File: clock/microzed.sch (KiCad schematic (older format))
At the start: 2 parts

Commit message: Update parts with parameter detail and BOM information.
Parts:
- PX1, PX2: Manufacturer (none) -> FCI; PartNum (none) -> 61083-101400LF
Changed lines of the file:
@@
 $Descr A4 11693 8268
 encoding utf-8
-Sheet 5 5
+Sheet 4 5
 Title ""
 Date ""
@@
 Comment4 ""
 $EndDescr
-$Comp
-L 61083_02X50 PX2
-U 1 1 5623D9A9
-P 5250 3750
-F 0 "PX2" H 5250 6400 50  0000 C CNN
-F 1 "61083_02X50" V 5250 3750 50  0000 C CNN
-F 2 "" H 5200 4250 60  0000 C CNN
-F 3 "" H 5200 4250 60  0000 C CNN
-	1    5250 3750
-	1    0    0    -1
-$EndComp
-$Comp
-L 61083_02X50 PX1
-U 1 1 5623D9E8
-P 2300 3750
-F 0 "PX1" H 2300 6400 50  0000 C CNN
-F 1 "61083_02X50" V 2300 3750 50  0000 C CNN
-F 2 "" H 2250 4250 60  0000 C CNN
-F 3 "" H 2250 4250 60  0000 C CNN
-	1    2300 3750
-	1    0    0    -1
-$EndComp
 $Comp
 L GND #PWR?
@@
 NoConn ~ 2000 5700
 NoConn ~ 2000 5600
+$Comp
+L 61083_02X50 PX2
+U 1 1 5633065B
+P 5250 3750
+F 0 "PX2" H 5250 6400 50  0000 C CNN
+F 1 "61083_02X50" V 5250 3750 50  0000 C CNN
+F 2 "" H 5200 4250 60  0000 C CNN
+F 3 "" H 5200 4250 60  0000 C CNN
+F 4 "FCI" H 5250 6600 50  0001 C CNN "Manufacturer"
+F 5 "61083-101400LF" H 5250 6500 50  0001 C CNN "PartNum"
+	1    5250 3750
+	1    0    0    -1
+$EndComp
+$Comp
+L 61083_02X50 PX1
+U 1 1 5633070F
+P 2300 3750
+F 0 "PX1" H 2300 6400 50  0000 C CNN
+F 1 "61083_02X50" V 2300 3750 50  0000 C CNN
+F 2 "" H 2250 4250 60  0000 C CNN
+F 3 "" H 2250 4250 60  0000 C CNN
+F 4 "FCI" H 2300 6600 50  0001 C CNN "Manufacturer"
+F 5 "61083-101400LF" H 2300 6500 50  0001 C CNN "PartNum"
+	1    2300 3750
+	1    0    0    -1
+$EndComp
 $EndSCHEMATC

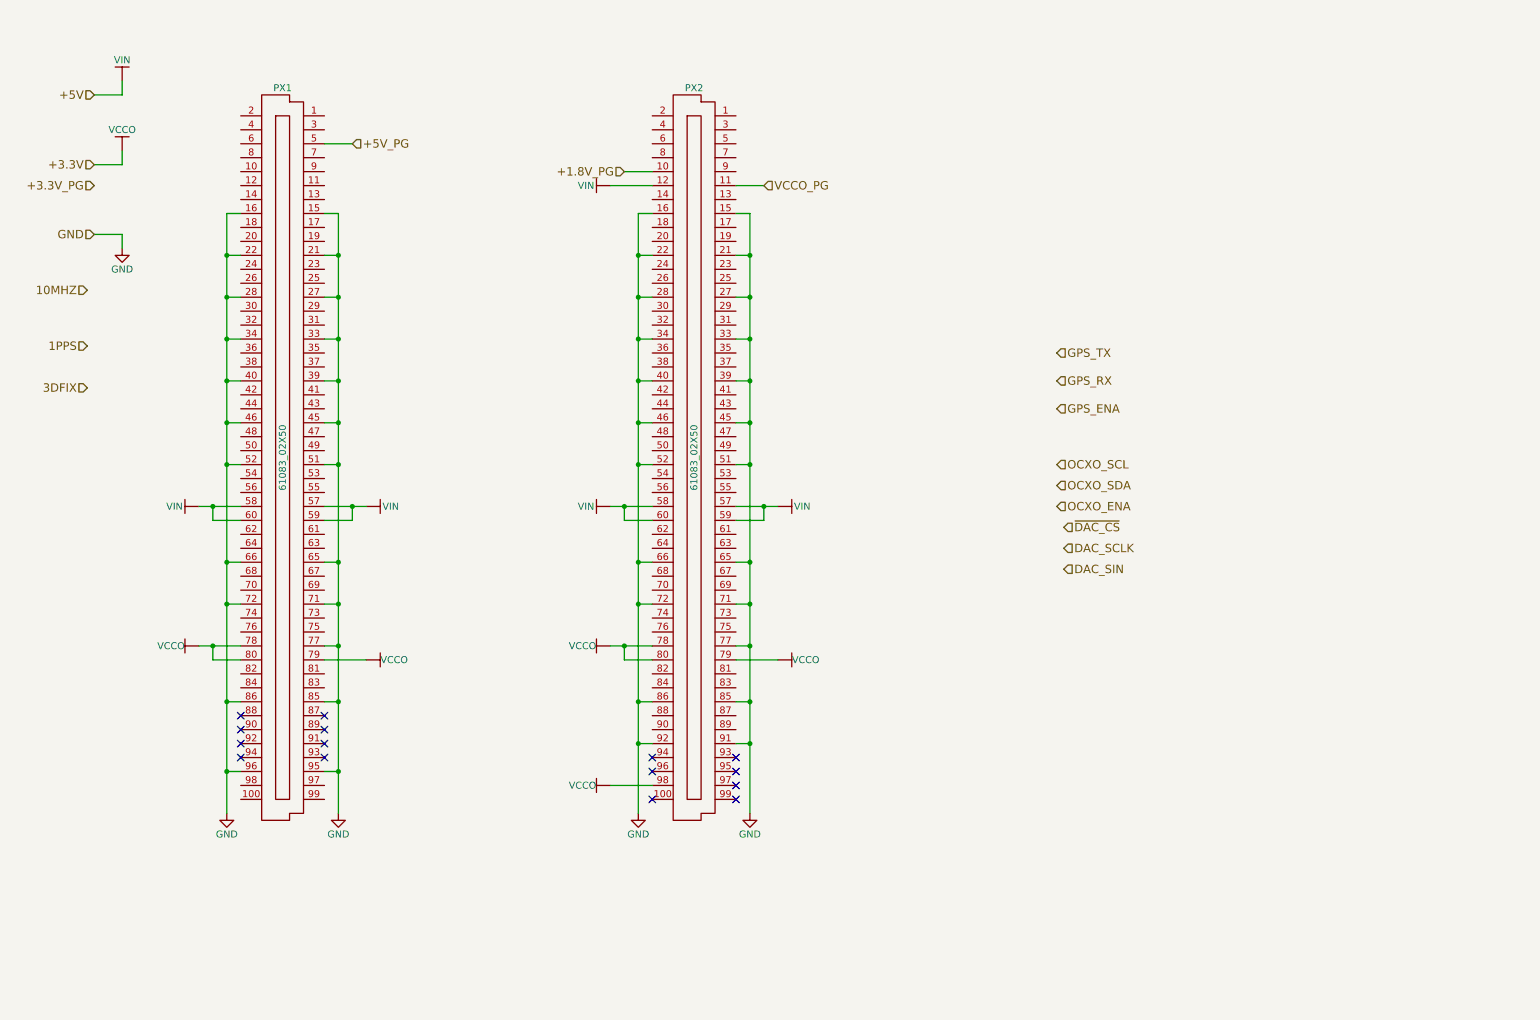
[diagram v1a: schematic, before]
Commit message: Add sheet for RTC and temperature sensors.
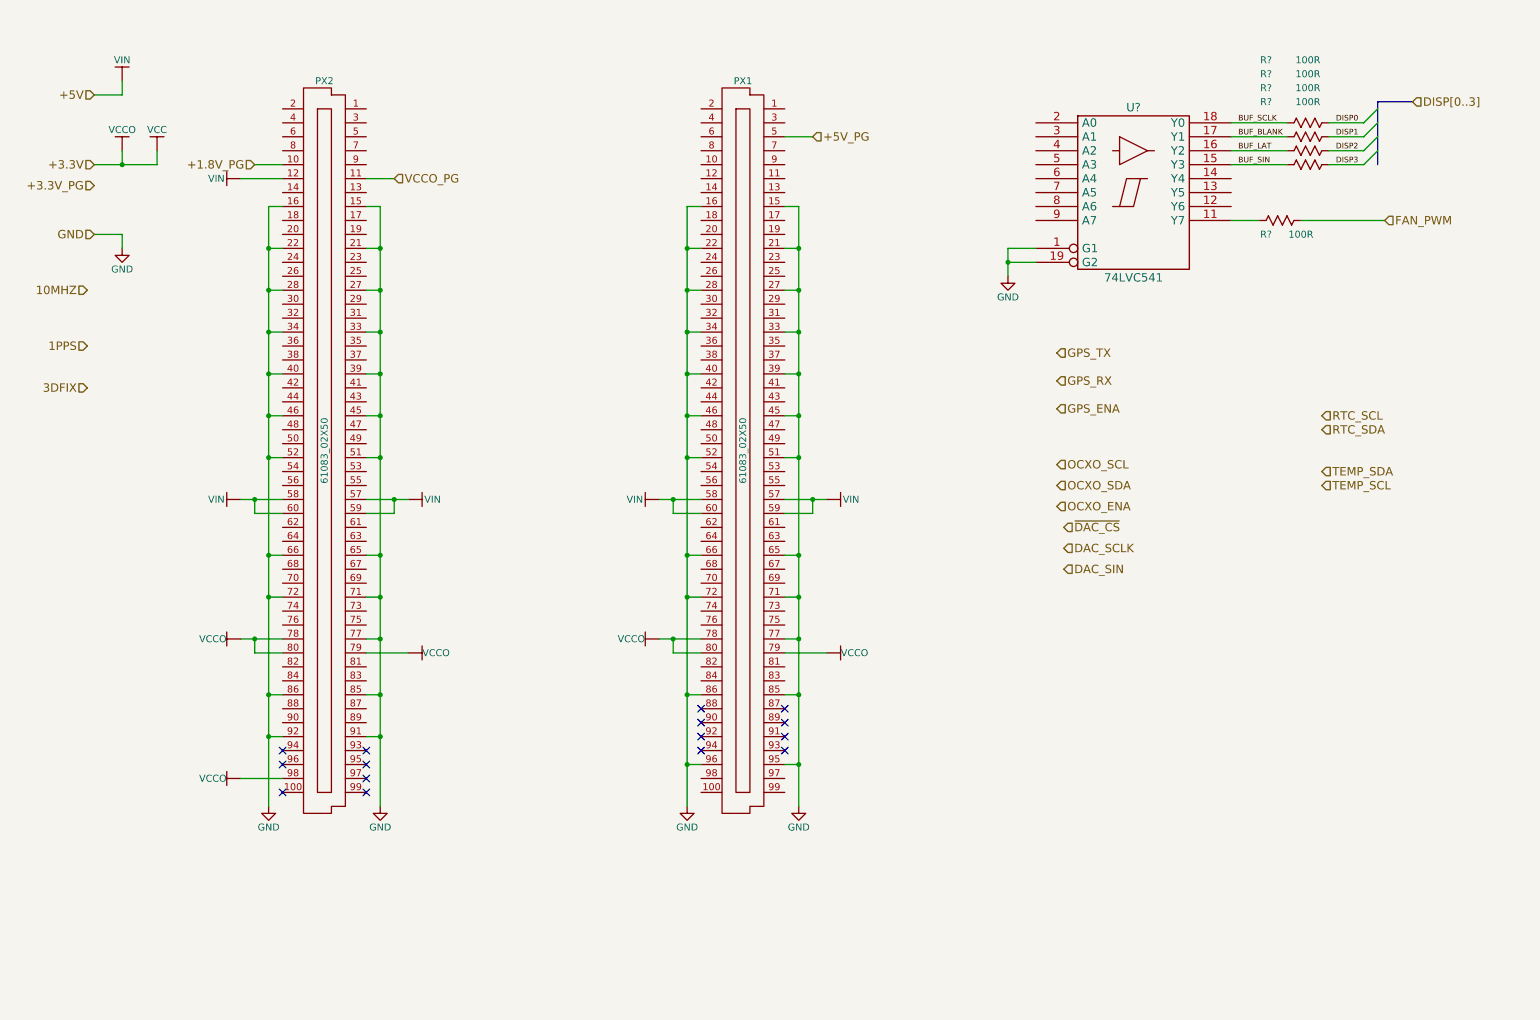
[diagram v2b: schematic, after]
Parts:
- added R? (x5): 100R, Resistors_SMD:R_0805_HandSoldering, symbol R_local
- added U?: 74LVC541, symbol 74LVC541
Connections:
- net GND: now also U?.1 (G1), U?.10 (GND), U?.19 (G2)
- net VCCO renamed VCC
- net VCC: now also U?.20 (VCC)
- new net: R?.2, U?.11 (Y7)
- new net BUF_BLANK: R?.2, U?.17 (Y1)
- new net BUF_LAT: R?.2, U?.16 (Y2)
- new net BUF_SCLK: R?.2, U?.18 (Y0)
- new net BUF_SIN: R?.2, U?.15 (Y3)
- new net DISP0: R?.1
- new net DISP1: R?.1
- new net DISP2: R?.1
- new net DISP3: R?.1
- new net FAN_PWM: R?.1
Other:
- moved on the sheet: PX1, PX2

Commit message: Fan and power connectors.
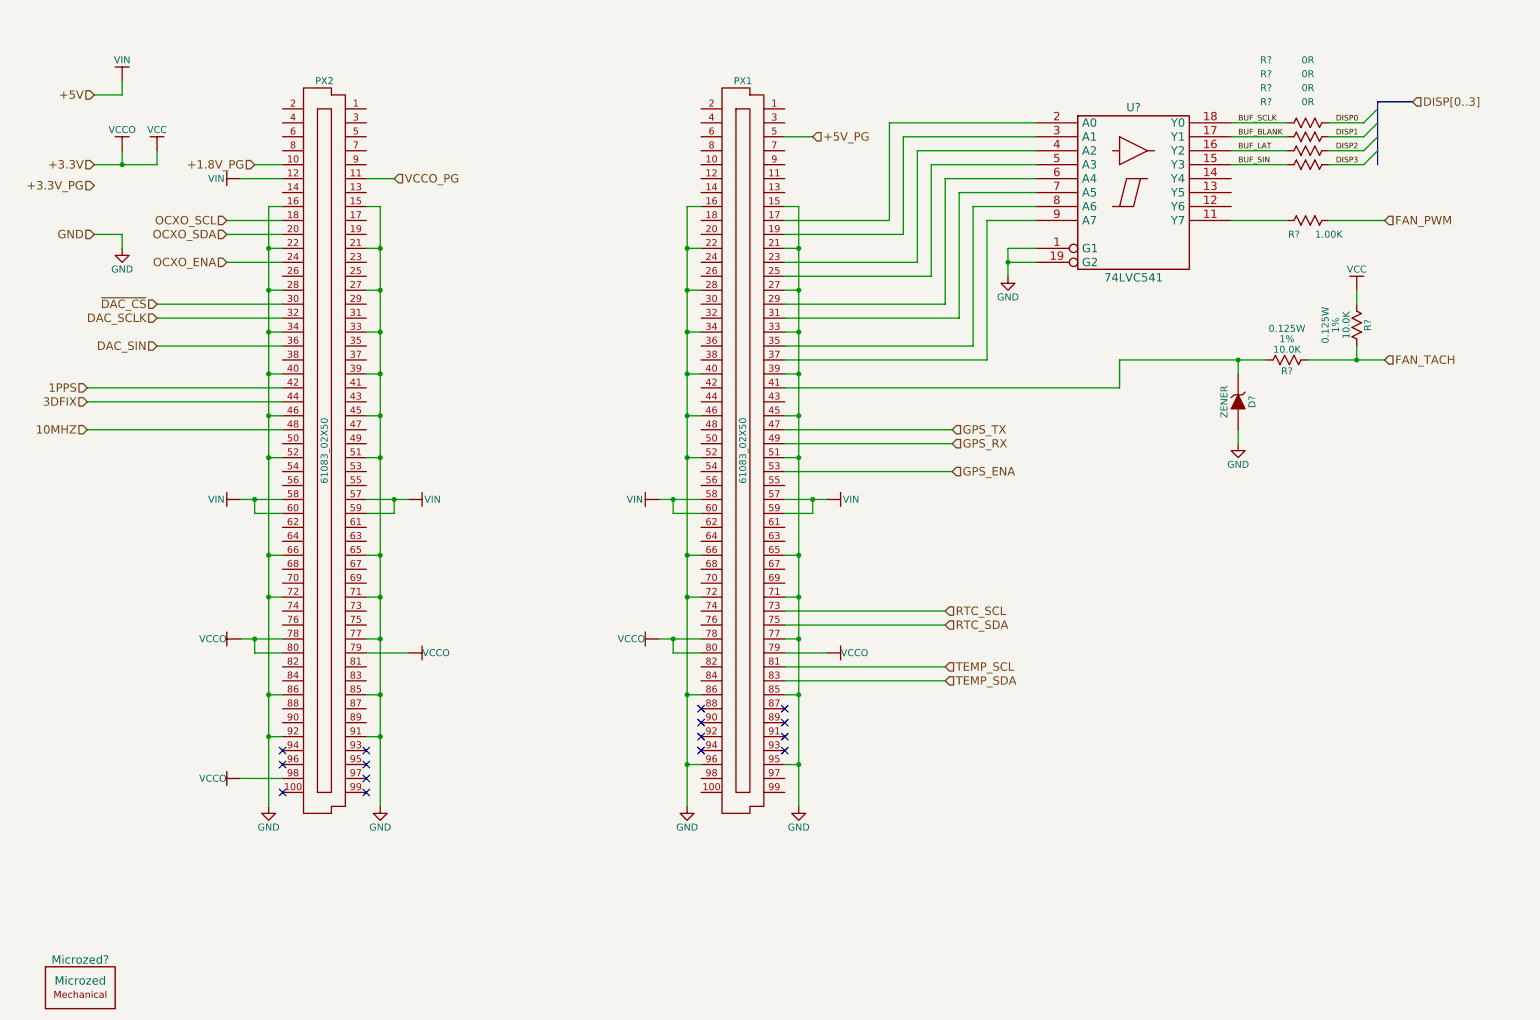
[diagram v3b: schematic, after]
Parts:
- removed R? (x3): 100R, Resistors_SMD:R_0805_HandSoldering, symbol R_local
- added D?: ZENER, symbol ZENER
- added Microzed?: Microzed, symbol Microzed
- added R? (x2): 10.0K, Resistors_SMD:R_0805_HandSoldering, symbol R_local
- added R? (x3): 0R, Resistors_SMD:R_0805_HandSoldering, symbol R_local
- R?: value 100R -> 0R; PartNum CRCW0805100RFKEA -> CRCW08050000Z0EA
- R?: value 100R -> 1.00K; PartNum CRCW0805100RFKEA -> CRCW08051K00FKEA
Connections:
- net 10MHZ: now also PX2.48
- net 1PPS: now also PX2.42
- net 3DFIX: now also PX2.44
- net BUF_BLANK: now also R?.2
- net BUF_LAT: now also R?.2
- net BUF_SIN: now also R?.2
- net DAC_SCLK: now also PX2.32
- net DAC_SIN: now also PX2.36
- net DISP1: now also R?.1
- net DISP2: now also R?.1
- net DISP3: now also R?.1
- net GND: now also D?.2 (A)
- net GPS_ENA: now also PX1.53
- net GPS_RX: now also PX1.49
- net GPS_TX: now also PX1.47
- net OCXO_ENA: now also PX2.24
- net OCXO_SCL: now also PX2.18
- net OCXO_SDA: now also PX2.20
- net RTC_SCL: now also PX1.73
- net RTC_SDA: now also PX1.75
- net TEMP_SCL: now also PX1.81
- net TEMP_SDA: now also PX1.83
- net VCC: now also R?.1
- net ~DAC_CS~: now also PX2.30
- net at PX1.17: now also U?.2 (A0)
- net at PX1.19: now also U?.3 (A1)
- net at PX1.23: now also U?.4 (A2)
- net at PX1.25: now also U?.5 (A3)
- net at PX1.29: now also U?.6 (A4)
- net at PX1.31: now also U?.7 (A5)
- net at PX1.35: now also U?.8 (A6)
- net at PX1.37: now also U?.9 (A7)
- net at PX1.41: now also D?.1 (K), R?.2
- new net FAN_TACH: R?.1, R?.2
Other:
- moved on the sheet: R?

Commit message: Correct footprint selection. Start pcb. Add BOM files.
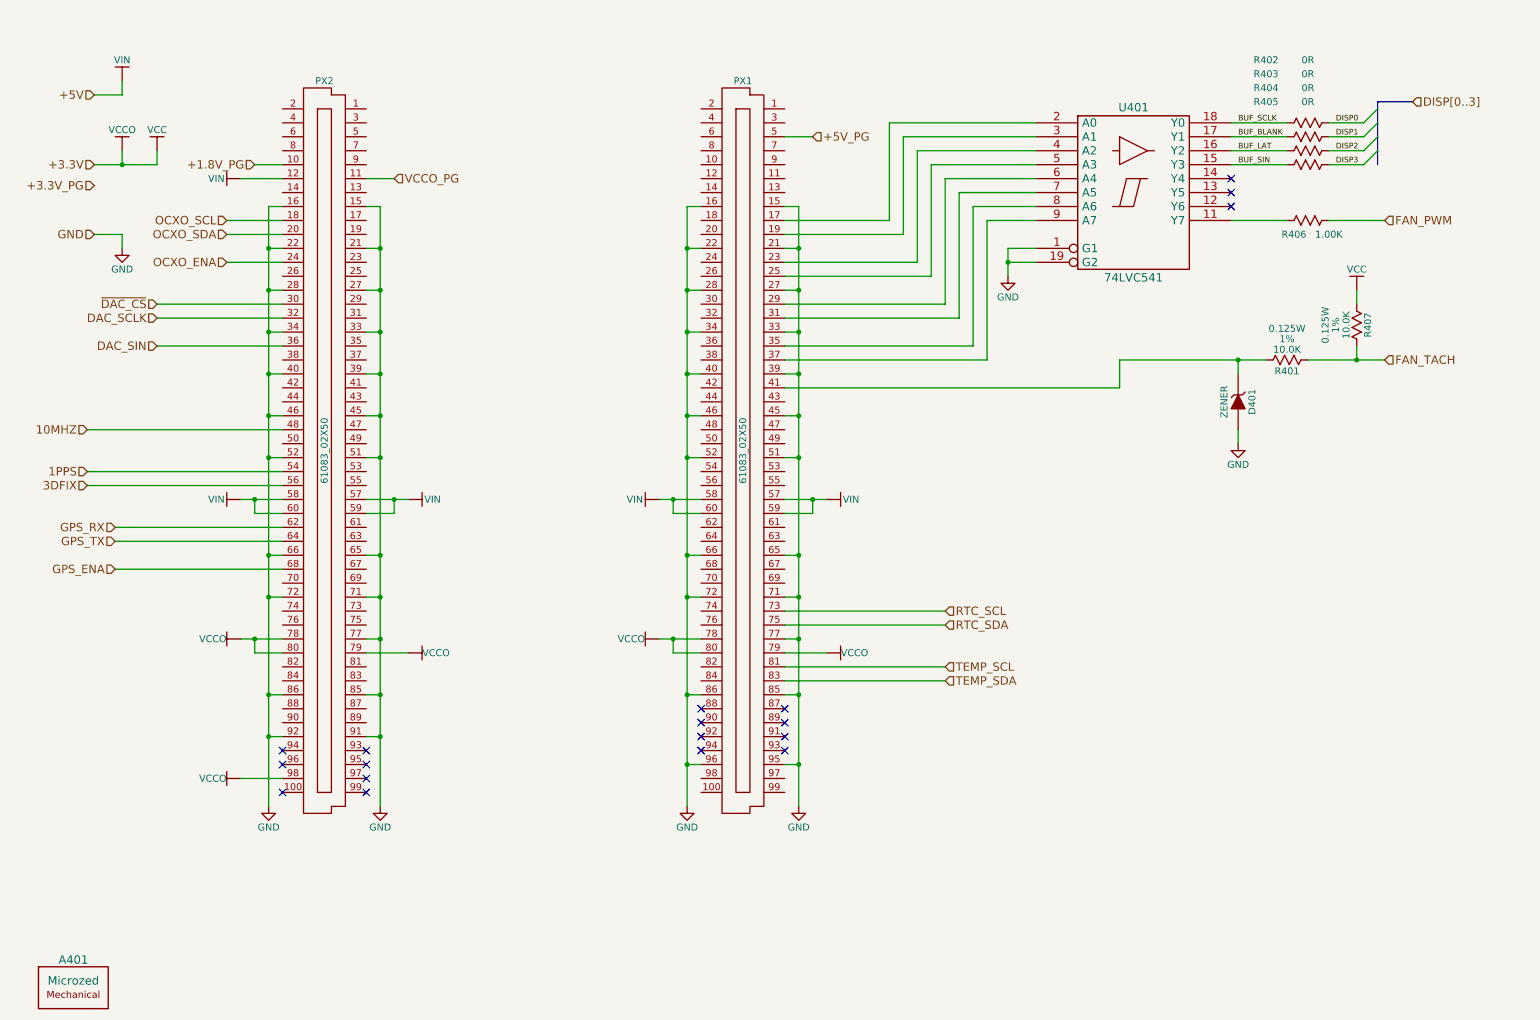
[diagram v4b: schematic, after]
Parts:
- removed Microzed?: Microzed, symbol Microzed
- added A401: Microzed, local:Microzed_RevF, symbol Microzed
- D401: renamed from D?; footprint (none) -> Diodes_SMD:SOD-123
- PX1, PX2: footprint (none) -> local:61083-2X50-SMD_HandSoldering
- U401: renamed from U?; footprint (none) -> Housings_SSOP:TSSOP-20_4.4x6.5mm_Pitch0.65mm
- gave numbers to parts that had none: 7
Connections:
- net 1PPS: now also PX2.54; no longer PX2.42
- net 3DFIX: now also PX2.56; no longer PX2.44
- net GPS_ENA: now also PX2.68; no longer PX1.53
- net GPS_RX: now also PX2.62; no longer PX1.49
- net GPS_TX: now also PX2.64; no longer PX1.47
- no-connect marks 15 -> 18
